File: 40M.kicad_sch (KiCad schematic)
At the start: 13 parts, among them Q5 MMBT2222A

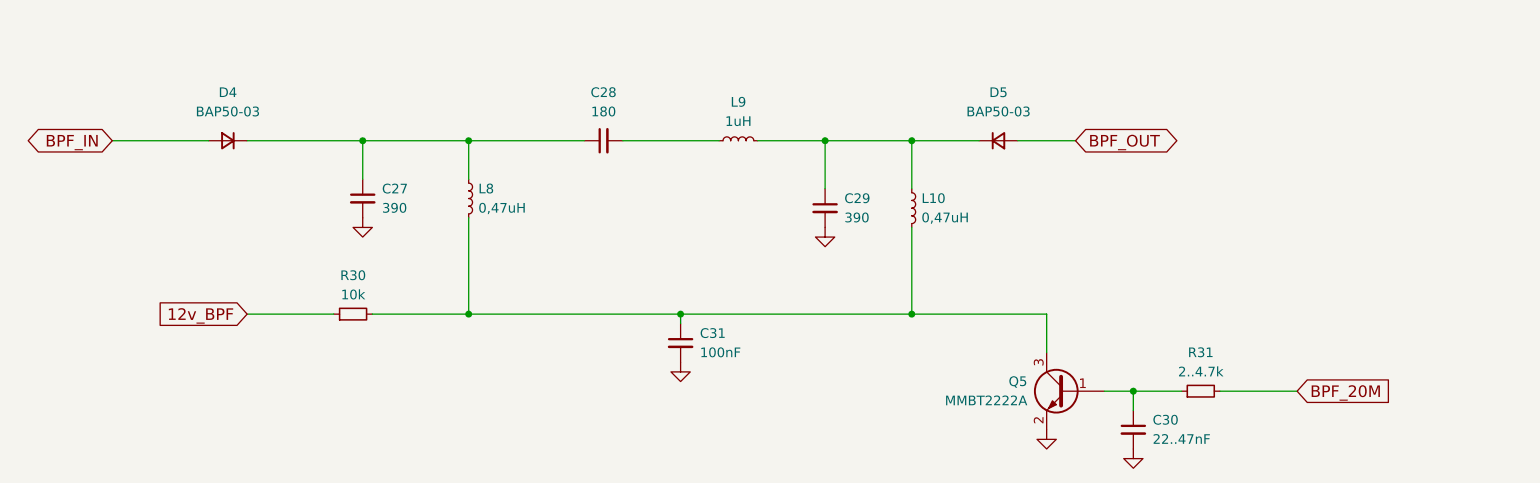
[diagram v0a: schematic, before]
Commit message: add custom footprints, progress on schema and PCB
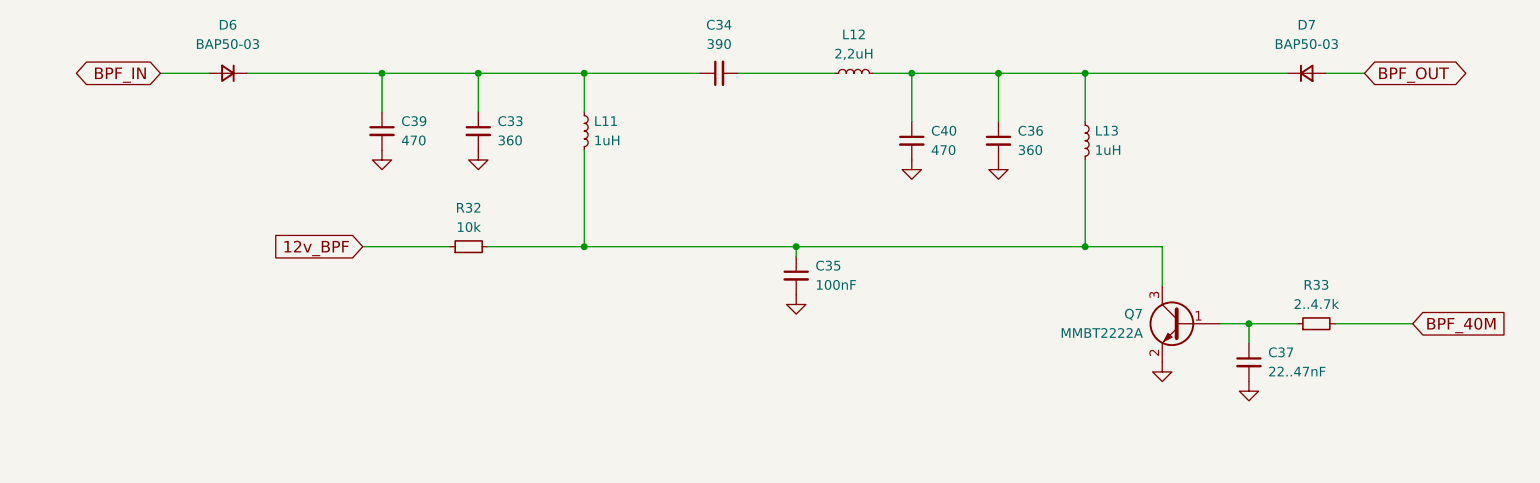
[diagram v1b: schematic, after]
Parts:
- removed C27, C29: 390, SDR_footprints:C_1206_0603, symbol Device:C_Small
- removed C28: 180, SDR_footprints:C_1206_0603, symbol Device:C_Small
- removed C30: 22..47nF, SDR_footprints:C_1206_0603, symbol Device:C_Small
- removed C31: 100nF, SDR_footprints:C_1206_0603, symbol Device:C_Small
- removed D4, D5: BAP50-03, Diode_SMD:D_SOD-323_HandSoldering, symbol Device:D_Small
- removed L10, L8: 0,47uH, SDR_footprints:Resistor_SMD+THTuniversal_0603to2512_RM10_HandSoldering, symbol Device:L_Small
- removed L9: 1uH, SDR_footprints:Resistor_SMD+THTuniversal_0603to2512_RM10_HandSoldering, symbol Device:L_Small
- removed Q5: MMBT2222A, Package_TO_SOT_SMD:SOT-23, symbol Transistor_BJT:MMBT2222A
- removed R30: 10k, SDR_footprints:R_1206_0603, symbol Device:R_Small
- removed R31: 2..4.7k, SDR_footprints:R_1206_0603, symbol Device:R_Small
- added C33: 360, Capacitor_SMD:C_0603_1608Metric_Pad1.08x0.95mm_HandSolder, symbol Device:C_Small
- added C34: 390, SDR_footprints:C_1206_0603, symbol Device:C_Small
- added C35: 100nF, SDR_footprints:C_1206_0603, symbol Device:C_Small
- added C36: 360, SDR_footprints:C_1206_0603, symbol Device:C_Small
- added C37: 22..47nF, SDR_footprints:C_1206_0603, symbol Device:C_Small
- added C39: 470, Capacitor_SMD:C_0603_1608Metric_Pad1.08x0.95mm_HandSolder, symbol Device:C_Small
- added C40: 470, SDR_footprints:C_1206_0603, symbol Device:C_Small
- added D6, D7: BAP50-03, Diode_SMD:D_SOD-323_HandSoldering, symbol Device:D_Small
- added L11, L13: 1uH, SDR_footprints:Resistor_SMD+THTuniversal_0603to2512_RM10_HandSoldering, symbol Device:L_Small
- added L12: 2,2uH, SDR_footprints:Resistor_SMD+THTuniversal_0603to2512_RM10_HandSoldering, symbol Device:L_Small
- added Q7: MMBT2222A, Package_TO_SOT_SMD:SOT-23, symbol Transistor_BJT:MMBT2222A
- added R32: 10k, Resistor_SMD:R_0603_1608Metric_Pad0.98x0.95mm_HandSolder, symbol Device:R_Small
- added R33: 2..4.7k, symbol Device:R_Small
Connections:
- net 12v_BPF: now also R32.1
- net BPF_IN: now also D6.2 (A)
- net BPF_OUT: now also D7.2 (A)
- net GND: now also C33.2, C35.2, C36.2, C37.2, C39.2, C40.2, Q7.2 (E)
- new net: C36.1, C40.1, D7.1 (K), L12.2, L13.1
- new net: C37.1, Q7.1 (B), R33.1
- new net: C35.1, L11.2, L13.2, Q7.3 (C), R32.2
- new net: C33.1, C34.1, C39.1, D6.1 (K), L11.1
- new net: C34.2, L12.1
- new net BPF_40M: R33.2

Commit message: progress on PCB
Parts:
- C34: footprint SDR_footprints:C_1206_0603 -> Capacitor_SMD:C_0603_1608Metric_Pad1.08x0.95mm_HandSolder
- R33: footprint (none) -> SDR_footprints:R_1206_0603
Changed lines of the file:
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@@
 			)
 		)
-		(property "Footprint" "SDR_footprints:C_1206_0603"
+		(property "Footprint" "Capacitor_SMD:C_0603_1608Metric_Pad1.08x0.95mm_HandSolder"
 			(at 137.16 72.39 0)
 			(effects
@@
 			)
 		)
-		(property "Footprint" ""
+		(property "Footprint" "SDR_footprints:R_1206_0603"
 			(at 215.9 105.41 0)
 			(effects
